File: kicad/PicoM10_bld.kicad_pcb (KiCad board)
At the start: 6 copper layers, 8 x 10 mm, 20 parts, among them J1 Conn_Coaxial, U1 MIA-M10Q, U2 NCP160xMX

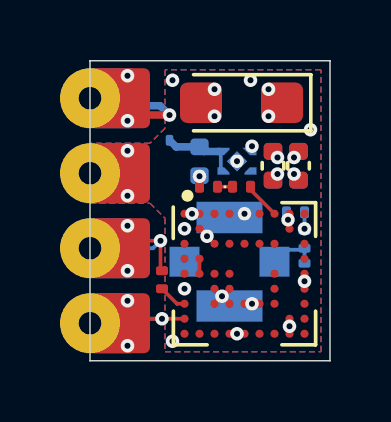
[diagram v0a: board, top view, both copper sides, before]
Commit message: add TVS diode
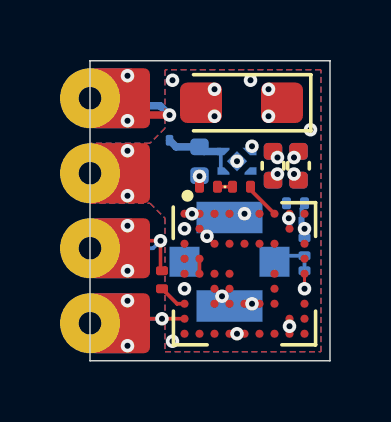
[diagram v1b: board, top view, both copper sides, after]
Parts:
- added D3: D_TVS, Diode_SMD:Nexperia_DSN0603-2_0.6x0.3mm_P0.4mm, B.Cu at (106.8, 105.3)
- U2: value NCP160xMX -> NCP160AMX330TBG
- moved L1 0.30 mm to (106.8, 104.8)
- moved C7 0.25 mm to (107.2, 106.2)
- moved L2 0.25 mm to (107.2, 107.3)
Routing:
- net Net-(D3-A2): track 0.60 -> 1.23 mm
